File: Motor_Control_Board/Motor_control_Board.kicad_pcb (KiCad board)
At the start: 4 copper layers, 76 x 32 mm, 99 parts, among them J1 TagConnect_TC2030, J10 C, J2 A, J3 Conn_01x02, J4 Encoder, J5 Encoder, J9 B, Q1 CSD18540Q5B, Q2 CSD18540Q5B, Q3 CSD18540Q5B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

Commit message: Minor updates: V0.9
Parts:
- added 5VDC: Jumper_2_Open, Jumper:SolderJumper-2_P1.3mm_Open_TrianglePad1.0x1.5mm, F.Cu at (131.9, 76.8)
- added C24: 470n, Capacitor_SMD:C_0603_1608Metric, B.Cu at (145.8, 57.6)
- added D3: SS12FP, Other:DIO_SS12LS_RVG, B.Cu at (149.2, 60.2)
- added R2: 10k, Resistor_SMD:R_0402_1005Metric, F.Cu at (140.0, 54.5)
- J5: value Encoder -> CAN
- moved C16 0.95 mm to (146.2, 59.8), turned to 90 degrees
- moved C18 0.20 mm to (135.8, 59.4)
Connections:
- J3 pad N: GND -> (no net)
- J3 pad P: +BATT -> (no net)
- J5 pad 1: +5V -> Net-(J5-Pin_1)
- U1 pad 40: unconnected-(U1-PB4-Pad40) -> DRV_FAULT
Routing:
- net GND: track 69.0 -> 76.8 mm, vias 69 -> 225
- net NRST: track 32.5 -> 39.1 mm
- net Net-(J5-Pin_1): track 0.00 -> 5.43 mm
- net Net-(U2-CP1): track 0.00 -> 4.11 mm
- net Net-(D3-K): track 2.28 -> 5.97 mm
- net DRV_FAULT: track 1.11 -> 4.55 mm
- net +3.3V: track 32.9 -> 35.6 mm, vias 10 -> 11
- net +24V: track 21.0 -> 23.7 mm
- net Net-(U2-CP2): track 0.00 -> 2.62 mm
- net +3.3VA: track 67.7 -> 66.3 mm

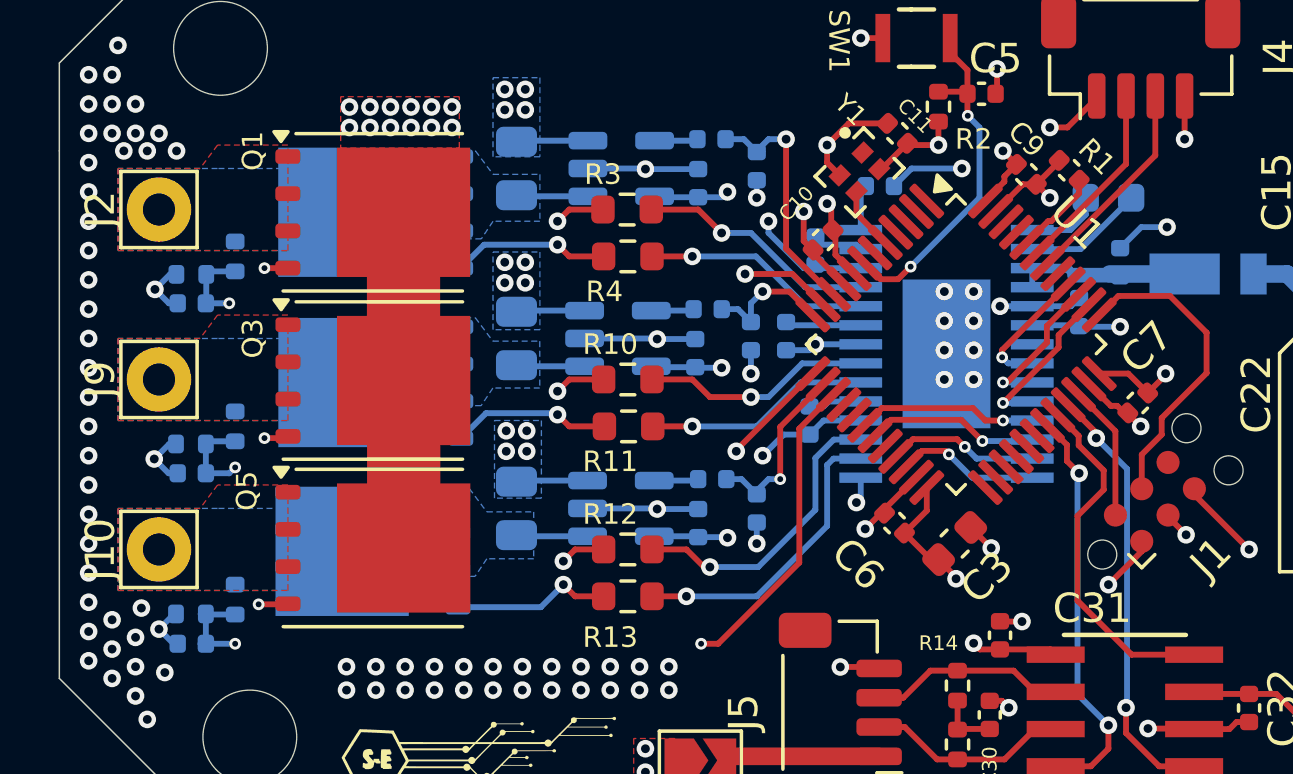
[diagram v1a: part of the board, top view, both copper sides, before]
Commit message: V0.10 - chnaged Volatge Sensing resistors to enable 48V sensing
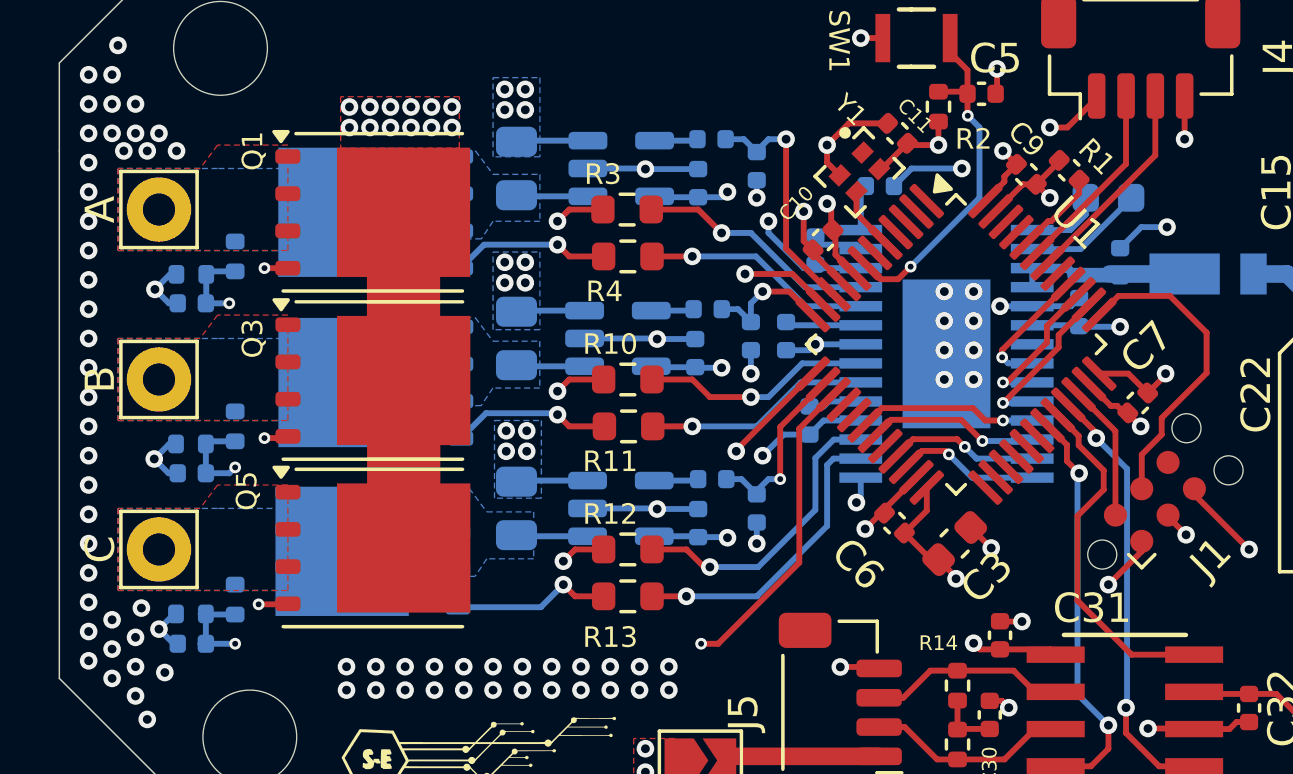
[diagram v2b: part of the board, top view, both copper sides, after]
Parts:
- renumbered J2 to A, J9 to B, J10 to C
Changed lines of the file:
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@@
 			(outputformat 1)
 			(mirror no)
-			(drillshape 1)
+			(drillshape 0)
 			(scaleselection 1)
-			(outputdirectory "")
+			(outputdirectory "../../../FabFiles/Motor Control Board/")
 		)
 	)
@@
 		(descr "solder Pin_ with flat fork, hole diameter 1.1mm, length 8.5mm, width 2.5mm")
 		(tags "solder Pin_ with flat fork")
-		(property "Reference" "J10"
+		(property "Reference" "C"
 			(at -2 0 90)
 			(layer "F.SilkS")
@@
 		(descr "solder Pin_ with flat fork, hole diameter 1.1mm, length 8.5mm, width 2.5mm")
 		(tags "solder Pin_ with flat fork")
-		(property "Reference" "J2"
+		(property "Reference" "A"
 			(at -2 0 90)
 			(layer "F.SilkS")
@@
 		(pad "1" smd roundrect
 			(at -4.1625 -2.75 315)
-			(size 1.475 0.3)
+			(size 1.475 0.28)
 			(layers "F.Cu" "F.Paste" "F.Mask")
 			(roundrect_rratio 0.25)
@@
 		(pad "2" smd roundrect
 			(at -4.1625 -2.25 315)
-			(size 1.475 0.3)
+			(size 1.475 0.28)
 			(layers "F.Cu" "F.Paste" "F.Mask")
 			(roundrect_rratio 0.25)
@@
 		(pad "3" smd roundrect
 			(at -4.1625 -1.75 315)
-			(size 1.475 0.3)
+			(size 1.475 0.28)
 			(layers "F.Cu" "F.Paste" "F.Mask")
 			(roundrect_rratio 0.25)
@@
 		(pad "4" smd roundrect
 			(at -4.1625 -1.249999 315)
-			(size 1.475 0.3)
+			(size 1.475 0.28)
 			(layers "F.Cu" "F.Paste" "F.Mask")
 			(roundrect_rratio 0.25)
@@
 		(pad "5" smd roundrect
 			(at -4.1625 -0.75 315)
-			(size 1.475 0.3)
+			(size 1.475 0.28)
 			(layers "F.Cu" "F.Paste" "F.Mask")
 			(roundrect_rratio 0.25)
@@
 		(pad "6" smd roundrect
 			(at -4.1625 -0.25 315)
-			(size 1.475 0.3)
+			(size 1.475 0.28)
 			(layers "F.Cu" "F.Paste" "F.Mask")
 			(roundrect_rratio 0.25)
@@
 		(pad "7" smd roundrect
 			(at -4.1625 0.25 315)
-			(size 1.475 0.3)
+			(size 1.475 0.28)
 			(layers "F.Cu" "F.Paste" "F.Mask")
 			(roundrect_rratio 0.25)
@@
 		(pad "8" smd roundrect
 			(at -4.1625 0.75 315)
-			(size 1.475 0.3)
+			(size 1.475 0.28)
 			(layers "F.Cu" "F.Paste" "F.Mask")
 			(roundrect_rratio 0.25)
@@
 		(pad "9" smd roundrect
 			(at -4.1625 1.249999 315)
-			(size 1.475 0.3)
+			(size 1.475 0.28)
 			(layers "F.Cu" "F.Paste" "F.Mask")
 			(roundrect_rratio 0.25)
@@
 		(pad "10" smd roundrect
 			(at -4.1625 1.75 315)
-			(size 1.475 0.3)
+			(size 1.475 0.28)
 			(layers "F.Cu" "F.Paste" "F.Mask")
 			(roundrect_rratio 0.25)
@@
 		(pad "11" smd roundrect
 			(at -4.1625 2.25 315)
-			(size 1.475 0.3)
+			(size 1.475 0.28)
 			(layers "F.Cu" "F.Paste" "F.Mask")
 			(roundrect_rratio 0.25)
@@
 		(pad "12" smd roundrect
 			(at -4.1625 2.75 315)
-			(size 1.475 0.3)
+			(size 1.475 0.28)
 			(layers "F.Cu" "F.Paste" "F.Mask")
 			(roundrect_rratio 0.25)
@@
 		(pad "13" smd roundrect
 			(at -2.75 4.1625 315)
-			(size 0.3 1.475)
+			(size 0.28 1.475)
 			(layers "F.Cu" "F.Paste" "F.Mask")
 			(roundrect_rratio 0.25)
@@
 		(pad "14" smd roundrect
 			(at -2.25 4.1625 315)
-			(size 0.3 1.475)
+			(size 0.28 1.475)
 			(layers "F.Cu" "F.Paste" "F.Mask")
 			(roundrect_rratio 0.25)
@@
 		(pad "15" smd roundrect
 			(at -1.75 4.1625 315)
-			(size 0.3 1.475)
+			(size 0.28 1.475)
 			(layers "F.Cu" "F.Paste" "F.Mask")
 			(roundrect_rratio 0.25)
@@
 		(pad "16" smd roundrect
 			(at -1.249999 4.1625 315)
-			(size 0.3 1.475)
+			(size 0.28 1.475)
 			(layers "F.Cu" "F.Paste" "F.Mask")
 			(roundrect_rratio 0.25)
@@
 		(pad "17" smd roundrect
 			(at -0.75 4.1625 315)
-			(size 0.3 1.475)
+			(size 0.28 1.475)
 			(layers "F.Cu" "F.Paste" "F.Mask")
 			(roundrect_rratio 0.25)
@@
 		(pad "18" smd roundrect
 			(at -0.25 4.1625 315)
-			(size 0.3 1.475)
+			(size 0.28 1.475)
 			(layers "F.Cu" "F.Paste" "F.Mask")
 			(roundrect_rratio 0.25)
@@
 		(pad "19" smd roundrect
 			(at 0.25 4.1625 315)
-			(size 0.3 1.475)
+			(size 0.28 1.475)
 			(layers "F.Cu" "F.Paste" "F.Mask")
 			(roundrect_rratio 0.25)
@@
 		(pad "20" smd roundrect
 			(at 0.75 4.1625 315)
-			(size 0.3 1.475)
+			(size 0.28 1.475)
 			(layers "F.Cu" "F.Paste" "F.Mask")
 			(roundrect_rratio 0.25)
@@
 		(pad "21" smd roundrect
 			(at 1.249999 4.1625 315)
-			(size 0.3 1.475)
+			(size 0.28 1.475)
 			(layers "F.Cu" "F.Paste" "F.Mask")
 			(roundrect_rratio 0.25)
@@
 		(pad "22" smd roundrect
 			(at 1.75 4.1625 315)
-			(size 0.3 1.475)
+			(size 0.28 1.475)
 			(layers "F.Cu" "F.Paste" "F.Mask")
 			(roundrect_rratio 0.25)
@@
 		(pad "23" smd roundrect
 			(at 2.25 4.1625 315)
-			(size 0.3 1.475)
+			(size 0.28 1.475)
 			(layers "F.Cu" "F.Paste" "F.Mask")
 			(roundrect_rratio 0.25)
@@
 		(pad "24" smd roundrect
 			(at 2.75 4.1625 315)
-			(size 0.3 1.475)
+			(size 0.28 1.475)
 			(layers "F.Cu" "F.Paste" "F.Mask")
 			(roundrect_rratio 0.25)
@@
 		(pad "25" smd roundrect
 			(at 4.1625 2.75 315)
-			(size 1.475 0.3)
+			(size 1.475 0.28)
 			(layers "F.Cu" "F.Paste" "F.Mask")
 			(roundrect_rratio 0.25)
@@
 		(pad "26" smd roundrect
 			(at 4.1625 2.25 315)
-			(size 1.475 0.3)
+			(size 1.475 0.28)
 			(layers "F.Cu" "F.Paste" "F.Mask")
 			(roundrect_rratio 0.25)
@@
 		(pad "27" smd roundrect
 			(at 4.1625 1.75 315)
-			(size 1.475 0.3)
+			(size 1.475 0.28)
 			(layers "F.Cu" "F.Paste" "F.Mask")
 			(roundrect_rratio 0.25)
@@
 		(pad "28" smd roundrect
 			(at 4.1625 1.249999 315)
-			(size 1.475 0.3)
+			(size 1.475 0.28)
 			(layers "F.Cu" "F.Paste" "F.Mask")
 			(roundrect_rratio 0.25)
@@
 		(pad "29" smd roundrect
 			(at 4.1625 0.75 315)
-			(size 1.475 0.3)
+			(size 1.475 0.28)
 			(layers "F.Cu" "F.Paste" "F.Mask")
 			(roundrect_rratio 0.25)
@@
 		(pad "30" smd roundrect
 			(at 4.1625 0.25 315)
-			(size 1.475 0.3)
+			(size 1.475 0.28)
 			(layers "F.Cu" "F.Paste" "F.Mask")
 			(roundrect_rratio 0.25)
@@
 		(pad "31" smd roundrect
 			(at 4.1625 -0.25 315)
-			(size 1.475 0.3)
+			(size 1.475 0.28)
 			(layers "F.Cu" "F.Paste" "F.Mask")
 			(roundrect_rratio 0.25)
@@
 		(pad "32" smd roundrect
 			(at 4.1625 -0.75 315)
-			(size 1.475 0.3)
+			(size 1.475 0.28)
 			(layers "F.Cu" "F.Paste" "F.Mask")
 			(roundrect_rratio 0.25)
@@
 		(pad "33" smd roundrect
 			(at 4.1625 -1.249999 315)
-			(size 1.475 0.3)
+			(size 1.475 0.28)
 			(layers "F.Cu" "F.Paste" "F.Mask")
 			(roundrect_rratio 0.25)
@@
 		(pad "34" smd roundrect
 			(at 4.1625 -1.75 315)
-			(size 1.475 0.3)
+			(size 1.475 0.28)
 			(layers "F.Cu" "F.Paste" "F.Mask")
 			(roundrect_rratio 0.25)
@@
 		(pad "35" smd roundrect
 			(at 4.1625 -2.25 315)
-			(size 1.475 0.3)
+			(size 1.475 0.28)
 			(layers "F.Cu" "F.Paste" "F.Mask")
 			(roundrect_rratio 0.25)
@@
 		(pad "36" smd roundrect
 			(at 4.1625 -2.75 315)
-			(size 1.475 0.3)
+			(size 1.475 0.28)
 			(layers "F.Cu" "F.Paste" "F.Mask")
 			(roundrect_rratio 0.25)
@@
 		(pad "37" smd roundrect
 			(at 2.75 -4.1625 315)
-			(size 0.3 1.475)
+			(size 0.28 1.475)
 			(layers "F.Cu" "F.Paste" "F.Mask")
 			(roundrect_rratio 0.25)
@@
 		(pad "38" smd roundrect
 			(at 2.25 -4.1625 315)
-			(size 0.3 1.475)
+			(size 0.28 1.475)
 			(layers "F.Cu" "F.Paste" "F.Mask")
 			(roundrect_rratio 0.25)
@@
 		(pad "39" smd roundrect
 			(at 1.75 -4.1625 315)
-			(size 0.3 1.475)
+			(size 0.28 1.475)
 			(layers "F.Cu" "F.Paste" "F.Mask")
 			(roundrect_rratio 0.25)
@@
 		(pad "40" smd roundrect
 			(at 1.249999 -4.1625 315)
-			(size 0.3 1.475)
+			(size 0.28 1.475)
 			(layers "F.Cu" "F.Paste" "F.Mask")
 			(roundrect_rratio 0.25)
@@
 		(pad "41" smd roundrect
 			(at 0.75 -4.1625 315)
-			(size 0.3 1.475)
+			(size 0.28 1.475)
 			(layers "F.Cu" "F.Paste" "F.Mask")
 			(roundrect_rratio 0.25)
@@
 		(pad "42" smd roundrect
 			(at 0.25 -4.1625 315)
-			(size 0.3 1.475)
+			(size 0.28 1.475)
 			(layers "F.Cu" "F.Paste" "F.Mask")
 			(roundrect_rratio 0.25)
@@
 		(pad "43" smd roundrect
 			(at -0.25 -4.1625 315)
-			(size 0.3 1.475)
+			(size 0.28 1.475)
 			(layers "F.Cu" "F.Paste" "F.Mask")
 			(roundrect_rratio 0.25)
@@
 		(pad "44" smd roundrect
 			(at -0.75 -4.1625 315)
-			(size 0.3 1.475)
+			(size 0.28 1.475)
 			(layers "F.Cu" "F.Paste" "F.Mask")
 			(roundrect_rratio 0.25)
@@
 		(pad "45" smd roundrect
 			(at -1.249999 -4.1625 315)
-			(size 0.3 1.475)
+			(size 0.28 1.475)
 			(layers "F.Cu" "F.Paste" "F.Mask")
 			(roundrect_rratio 0.25)
@@
 		(pad "46" smd roundrect
 			(at -1.75 -4.1625 315)
-			(size 0.3 1.475)
+			(size 0.28 1.475)
 			(layers "F.Cu" "F.Paste" "F.Mask")
 			(roundrect_rratio 0.25)
@@
 		(pad "47" smd roundrect
 			(at -2.25 -4.1625 315)
-			(size 0.3 1.475)
+			(size 0.28 1.475)
 			(layers "F.Cu" "F.Paste" "F.Mask")
 			(roundrect_rratio 0.25)
@@
 		(pad "48" smd roundrect
 			(at -2.75 -4.1625 315)
-			(size 0.3 1.475)
+			(size 0.28 1.475)
 			(layers "F.Cu" "F.Paste" "F.Mask")
 			(roundrect_rratio 0.25)
@@
 		(descr "solder Pin_ with flat fork, hole diameter 1.1mm, length 8.5mm, width 2.5mm")
 		(tags "solder Pin_ with flat fork")
-		(property "Reference" "J9"
+		(property "Reference" "B"
 			(at -2 0 90)
 			(layer "F.SilkS")
